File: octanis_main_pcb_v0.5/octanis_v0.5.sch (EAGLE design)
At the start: 78 parts, among them IC1 BME280, Q1 32.768kHz, Q2 32.768kHz, U3 DRV8836DSSR, U4 DRV8836DSSR, U5 DRV8836DSSR, U7 DRV8836DSSR

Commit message: rearranged GPIOs
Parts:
- removed C10: 4.7u, rcl:C-EUC0603
- removed C13: 220n, rcl:C-EUC0603
- removed C15: 100n, rcl:C-EUC0603
- removed COMPASS: HMC5883L, HMC5883L:HMC5883L
- removed GPIO1: A7:A0, pinhead:PINHD-1X8
- removed GPIO2: A18:A8, pinhead:PINHD-1X11
- added JP7: SPI, pinhead:PINHD-1X4
- added JP8: (no value), pinhead:PINHD-2X12
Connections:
- removed net N$14: GPIO2.1, MSP1.P4.5/A8
- removed net N$15: GPIO2.2, MSP1.P4.4/HSMCLK/SVMHOUT/A9
- removed net N$17: C10.1, COMPASS.C1
- removed net N$20: GPIO2.3, MSP1.P4.3/MCLK/RTCCLK/A10
- removed net N$21: GPIO2.4, MSP1.P4.2/ACLK/TA2CLK/A11
- removed net N$22: GPIO2.5, MSP1.P4.1/A12
- removed net N$23: GPIO2.6, MSP1.P4.0/A13
- removed net N$25: C13.2, COMPASS.SETP
- removed net N$27: GPIO1.1, MSP1.P5.5/A0
- removed net N$28: GPIO1.2, MSP1.P5.4/A1
- removed net N$30: GPIO1.3, MSP1.P5.3/A2
- removed net N$32: C13.1, COMPASS.SETC
- removed net N$35: GPIO1.4, MSP1.P5.2/A3
- removed net N$36: GPIO1.5, MSP1.P5.1/A4
- removed net N$37: GPIO1.6, MSP1.P5.0/A5
- removed net N$38: GPIO1.8, MSP1.P4.6/A7
- removed net N$43: GPIO1.7, MSP1.P4.7/A6
- new net A0: JP8.1, MSP1.P5.5/A0
- new net A1: JP8.2, MSP1.P5.4/A1
- new net A10: JP8.11, MSP1.P4.3/MCLK/RTCCLK/A10
- new net A11: JP8.12, MSP1.P4.2/ACLK/TA2CLK/A11
- new net A12: JP8.13, MSP1.P4.1/A12
- new net A13: JP8.14, MSP1.P4.0/A13
- new net A2: JP8.3, MSP1.P5.3/A2
- new net A23: JP8.24, MSP1.P8.2/TA3.2/A23
- new net A3: JP8.4, MSP1.P5.2/A3
- new net A4: JP8.5, MSP1.P5.1/A4
- new net A5: JP8.6, MSP1.P5.0/A5
- new net A6: JP8.7, MSP1.P4.7/A6
- new net A7: JP8.8, MSP1.P4.6/A7
- new net A8: JP8.9, MSP1.P4.5/A8
- new net A9: JP8.10, MSP1.P4.4/HSMCLK/SVMHOUT/A9
- net +3V3: no longer C15.2, COMPASS.S1, COMPASS.VDD, COMPASS.VDD_IO
- net A14: now also JP8.15; no longer GPIO2.7
- net A15: now also JP8.16; no longer GPIO2.8
- net A16: now also JP8.17; no longer GPIO2.9
- net A17: now also JP8.18; no longer GPIO2.10
- net A18: now also JP8.19; no longer GPIO2.11
- net A19: now also JP8.20
- net A20: now also JP8.21
- net A21: now also JP8.22
- net A22: now also JP8.23
- net GND: no longer C10.2, C15.1, COMPASS.GND
- net M5678SLEEP: now also MSP1.P2.0/PM_UCA1STE; no longer MSP1.P3.4/PM_UCB2STE
- net M7IN1: now also MSP1.P8.1/UCB3CLK/TA2.0/C0.0; no longer MSP1.P3.0/PM_UCA2STE
- net M7IN2: now also MSP1.P3.0/PM_UCA2STE; no longer MSP1.P8.1/UCB3CLK/TA2.0/C0.0
- net M8IN2: now also MSP1.P3.4/PM_UCB2STE; no longer MSP1.P8.2/TA3.2/A23
- net SCL: no longer COMPASS.SCL
- net SDA: no longer COMPASS.SDA
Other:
- note removed: "compass"

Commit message: separated motor supply. added pull ups for sleep pin
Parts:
- added R11, R12: 10k, rcl:R-EU_R0603
- added SJ6: (no value), jumper:SJ
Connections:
- new net V_MOTOR2: C26.2, C8.2, SJ6.1, U5.VCC, U7.VCC
- net +3V3: now also R11.2, R12.2
- net M1234SLEEP: now also R12.1
- net M5678SLEEP: now also R11.1
- net V_MOTOR: now also SJ6.2; no longer C26.2, C8.2, U5.VCC, U7.VCC
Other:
- moved on the sheet: C26, C27, C28, C29, C3, C4, C5, C6, C7, C8, IC1, JP4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

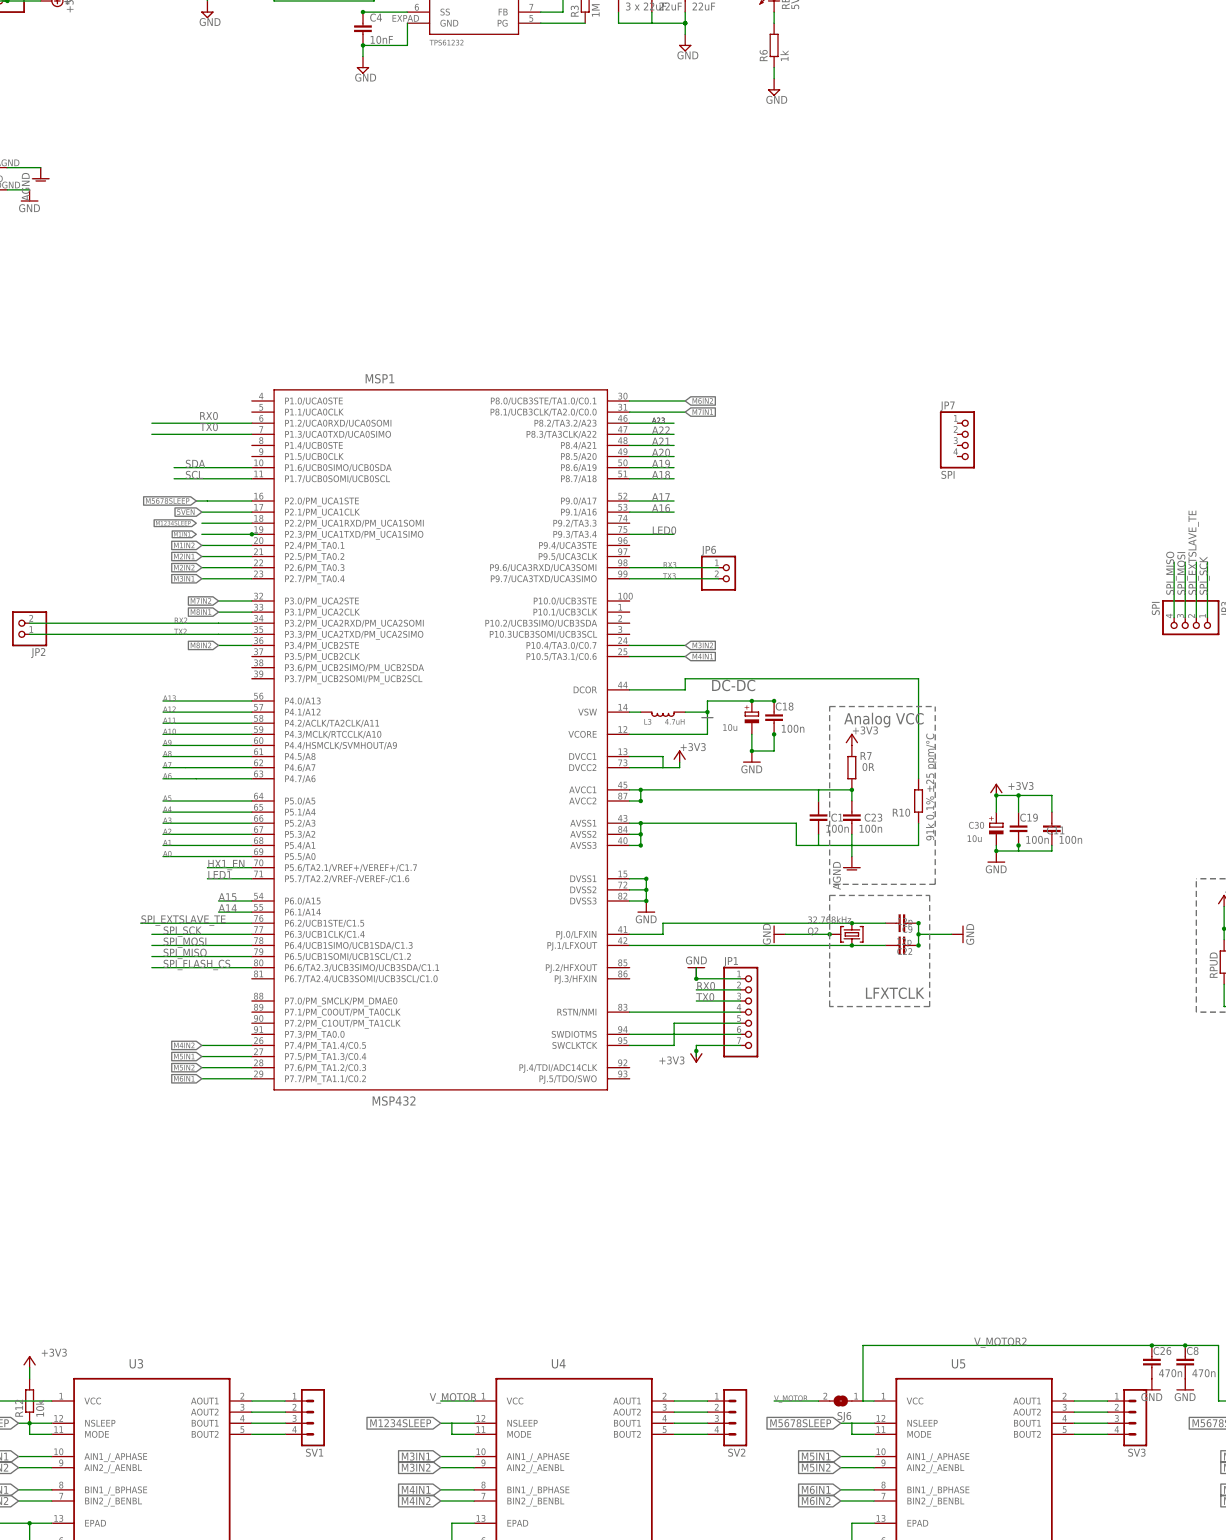
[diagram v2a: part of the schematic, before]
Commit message: redesigned hx1 pins
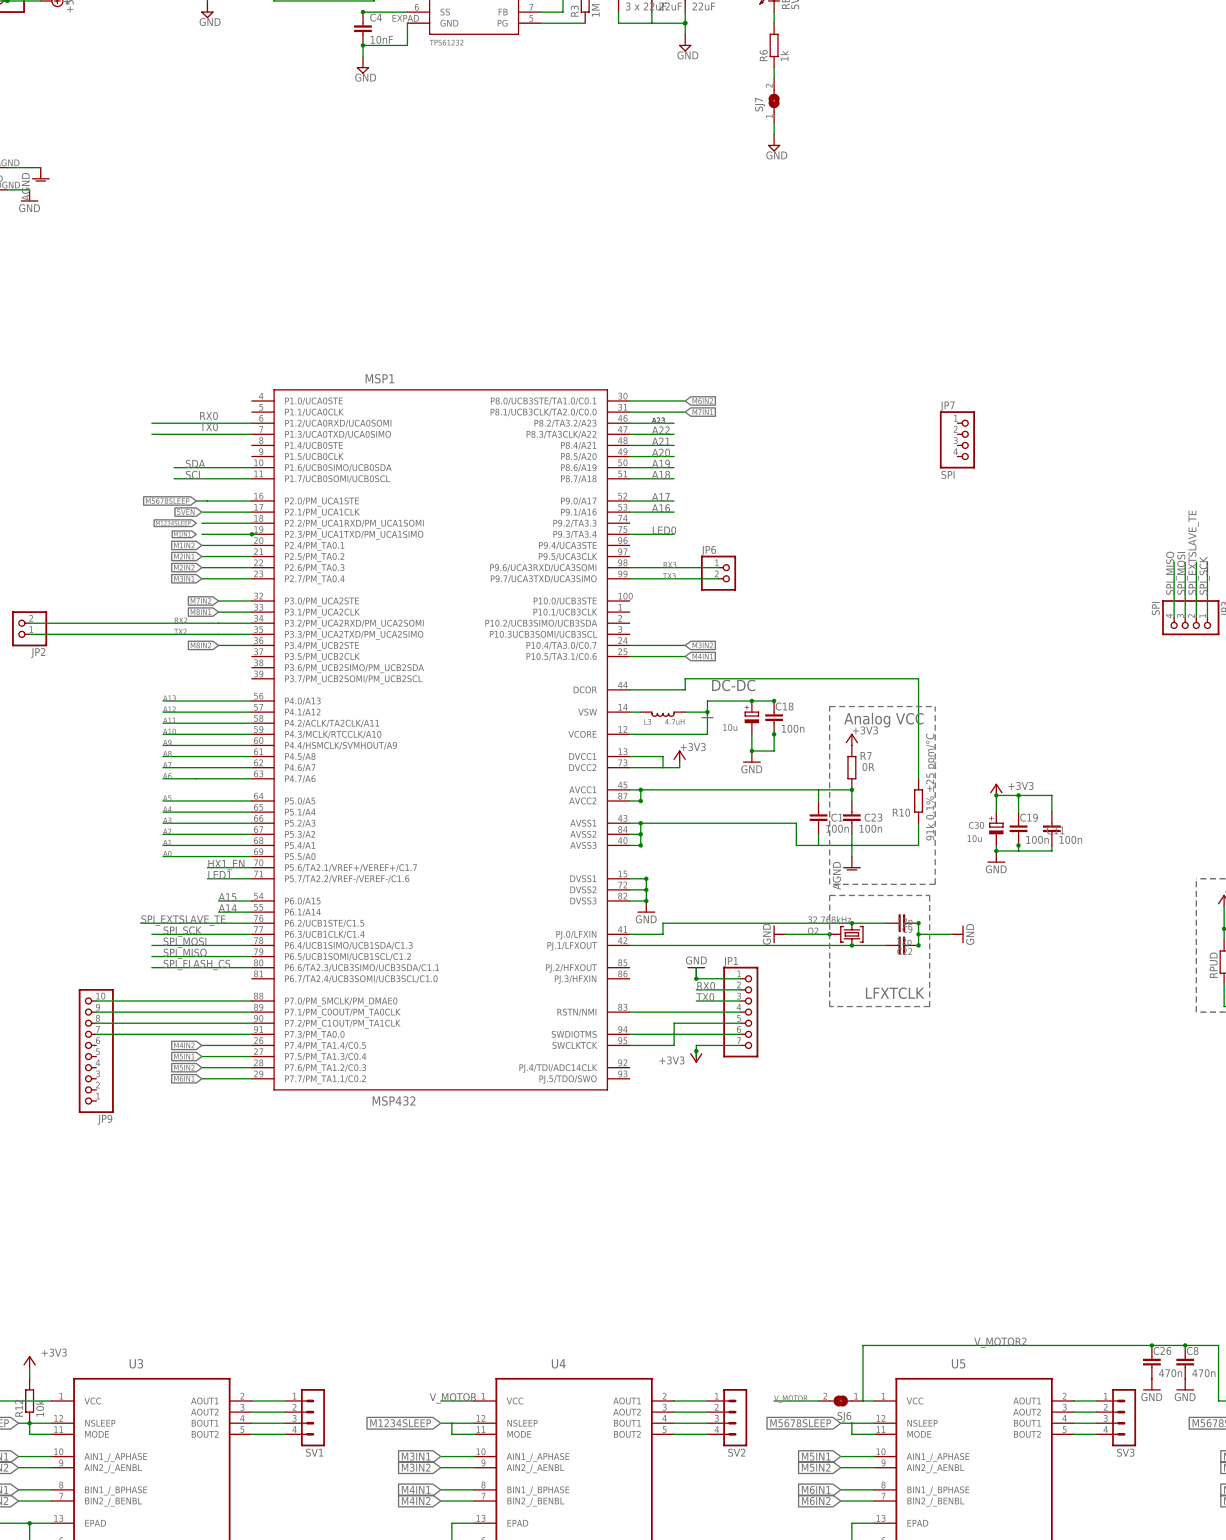
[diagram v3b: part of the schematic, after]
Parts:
- added JP9: (no value), pinhead:PINHD-1X10
- added SJ7: (no value), jumper:SJ
- U$4: value HX1 -> HX1EXTERNALMOUNT; device Octanis1:HX1 -> Octanis1:HX1EXTERNALMOUNT
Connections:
- new net N$14: R6.1, SJ7.2
- new net N$15: JP9.10, MSP1.P7.0/PM_SMCLK/PM_DMAE0
- new net N$17: JP9.9, MSP1.P7.1/PM_C0OUT/PM_TA0CLK
- new net N$20: JP9.8, MSP1.P7.2/PM_C1OUT/PM_TA1CLK
- new net N$21: JP9.7, MSP1.P7.3/PM_TA0.0
- net GND: now also SJ7.1; no longer R6.1
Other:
- moved on the sheet: SV3

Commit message: assigned all GPIO
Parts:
- removed JP2: (no value), pinhead:PINHD-1X2
- removed SJ4, SJ5: (no value), jumper:SJ
- added C10: 10u, rcl:CPOL-EUA/3216-18R
- added JP10: (no value), pinhead:PINHD-2X10
- JP3: value SPI -> (none); device pinhead:PINHD-1X4 -> pinhead:PINHD-2X2
- JP6: device pinhead:PINHD-1X2 -> pinhead:PINHD-2X2
- JP9: device pinhead:PINHD-1X10 -> pinhead:PINHD-2X2
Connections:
- removed net N$24: U$4.TXD
- removed net N$29: R8.1, SJ4.2
- removed net N$31: R9.1, SJ5.2
- new net HX1_DATA: MSP1.P1.4/UCB0STE, U$4.TXD
- new net P1.0: JP10.20, MSP1.P1.0/UCA0STE
- new net P1.1: JP10.19, MSP1.P1.1/UCA0CLK
- new net P10.2: JP10.17, MSP1.P10.2/UCB3SIMO/UCB3SDA
- new net P10.3: JP10.18, MSP1.P10.3UCB3SOMI/UCB3SCL
- new net P5.6: JP10.7, MSP1.P5.6/TA2.1/VREF+/VEREF+/C1.7
- new net P5.7: JP10.5, MSP1.P5.7/TA2.2/VREF-/VEREF-/C1.6
- new net P6.6: JP10.10, MSP1.P6.6/TA2.3/UCB3SIMO/UCB3SDA/C1.1
- new net P6.7: JP10.9, MSP1.P6.7/TA2.4/UCB3SOMI/UCB3SCL/C1.0
- new net P9.2: JP10.3, MSP1.P9.2/TA3.3
- new net P9.3: JP10.1, MSP1.P9.3/TA3.4
- new net P9.4: JP10.15, MSP1.P9.4/UCA3STE
- new net P9.5: JP10.16, MSP1.P9.5/UCA3CLK
- new net PJ.2: JP10.13, MSP1.PJ.2/HFXOUT
- new net PJ.3: JP10.14, MSP1.PJ.3/HFXIN
- new net PJ.4: JP10.11, MSP1.PJ.4/TDI/ADC14CLK
- new net PJ.5: JP10.12, MSP1.PJ.5/TDO/SWO
- net +3V3: now also JP6.1
- net +5V: now also C10.+, JP3.2
- net GND: now also JP3.4, JP6.3, R8.1, R9.1; no longer C2.2, SJ4.1, SJ5.1, U$4.0V
- net HX1_EN: now also MSP1.P1.5/UCB0CLK; no longer MSP1.P5.6/TA2.1/VREF+/VEREF+/C1.7
- net LED0: now also MSP1.P10.0/UCB3STE; no longer MSP1.P9.3/TA3.4
- net LED1: now also MSP1.P10.1/UCB3CLK; no longer MSP1.P5.7/TA2.2/VREF-/VEREF-/C1.6
- net N$15: now also JP10.2; no longer JP9.10
- net N$17: now also JP10.4; no longer JP9.9
- net N$19: now also Q1.2
- net N$20: now also JP10.6; no longer JP9.8
- net N$21: now also JP10.8; no longer JP9.7
- net RFGND: now also C10.-, C2.2, U$4.0V
- net RX2: now also JP6.2; no longer JP2.2
- net RX3: now also JP3.1; no longer JP6.1
- net SCL: now also JP4.1, JP5.3; no longer JP4.2, JP5.4
- net SDA: now also JP4.2, JP5.4; no longer JP4.1, JP5.3
- net SPI_EXTSLAVE_TE: now also JP9.1; no longer JP3.2
- net SPI_FLASH_CS: now also MSP1.P3.5/PM_UCB2CLK; no longer MSP1.P6.6/TA2.3/UCB3SIMO/UCB3SDA/C1.1
- net SPI_MISO: now also JP9.2; no longer JP3.4
- net SPI_MOSI: now also JP9.4; no longer JP3.3
- net SPI_SCK: now also JP9.3; no longer JP3.1
- net TX2: now also JP6.4; no longer JP2.1
- net TX3: now also JP3.3; no longer JP6.2
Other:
- note added: "Change history v0.5: --> SCHEMATIC: - added 10uF cap - connected 0V pin to RF GND - connected filter caps to RF GND --> LAYOUT: - Starground connection point placed directly at the supply pin. - Groundplane polygon around all pins with greater isolation space."
- moved on the sheet: JP3

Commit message: mainboard: digital gpio routed
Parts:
- removed JP10: (no value), pinhead:PINHD-2X10
- added C13: 100n, rcl:C-EUC0603
- added JP2: (no value), pinhead:PINHD-2X11
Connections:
- removed net 3.3V: U$3.WP
- removed net N$15: JP10.2, MSP1.P7.0/PM_SMCLK/PM_DMAE0
- removed net N$17: JP10.4, MSP1.P7.1/PM_C0OUT/PM_TA0CLK
- removed net N$20: JP10.6, MSP1.P7.2/PM_C1OUT/PM_TA1CLK
- removed net N$21: JP10.8, MSP1.P7.3/PM_TA0.0
- new net P3.6: JP2.5, MSP1.P3.6/PM_UCB2SIMO/PM_UCB2SDA
- new net P3.7: JP2.6, MSP1.P3.7/PM_UCB2SOMI/PM_UCB2SCL
- new net P7.0: JP2.12, MSP1.P7.0/PM_SMCLK/PM_DMAE0
- new net P7.1: JP2.11, MSP1.P7.1/PM_C0OUT/PM_TA0CLK
- new net P7.2: JP2.14, MSP1.P7.2/PM_C1OUT/PM_TA1CLK
- new net P7.3: JP2.13, MSP1.P7.3/PM_TA0.0
- net +3V3: now also C13.1, U$3.WP
- net GND: now also C13.2
- net P1.0: now also JP2.19; no longer JP10.20
- net P1.1: now also JP2.21; no longer JP10.19
- net P10.2: now also JP2.20; no longer JP10.17
- net P10.3: now also JP2.22; no longer JP10.18
- net P5.6: now also JP2.2; no longer JP10.7
- net P5.7: now also JP2.1; no longer JP10.5
- net P6.6: now also JP2.8; no longer JP10.10
- net P6.7: now also JP2.7; no longer JP10.9
- net P9.2: now also JP2.4; no longer JP10.3
- net P9.3: now also JP2.3; no longer JP10.1
- net P9.4: now also JP2.18; no longer JP10.15
- net P9.5: now also JP2.17; no longer JP10.16
- net PJ.2: now also JP2.10; no longer JP10.13
- net PJ.3: now also JP2.9; no longer JP10.14
- net PJ.4: now also JP2.16; no longer JP10.11
- net PJ.5: now also JP2.15; no longer JP10.12

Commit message: mainboard routing finished
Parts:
- removed JP7: SPI, pinhead:PINHD-1X4
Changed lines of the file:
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@@
 <part name="+3V19" library="supply1" deviceset="+3V3" device=""/>
 <part name="GND30" library="supply1" deviceset="GND" device=""/>
-<part name="JP7" library="pinhead" deviceset="PINHD-1X4" device="" value="SPI"/>
 <part name="JP8" library="pinhead" deviceset="PINHD-2X12" device=""/>
 <part name="+3V5" library="supply1" deviceset="+3V3" device=""/>
@@
 <instance part="+3V19" gate="G$1" x="828.04" y="210.82"/>
 <instance part="GND30" gate="1" x="833.12" y="114.3"/>
-<instance part="JP7" gate="A" x="450.85" y="327.66"/>
 <instance part="JP8" gate="A" x="190.5" y="248.92"/>
 <instance part="+3V5" gate="G$1" x="236.22" y="119.38" smashed="yes">

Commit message: mainboard finished
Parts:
- removed JP2: (no value), pinhead:PINHD-2X11
- removed JP3: (no value), pinhead:PINHD-2X2
- removed U$3: SST25VF064C, BertaLib:SST25VF064C
- added BLP, RST: PTR1B1,27, testpad:PTR1B1,27
- added DIGITAL_IO: (no value), pinhead:PINHD-2X11
- added RX3/TX3: (no value), pinhead:PINHD-2X2
- added U6: DRV8836DSSR, DRV8834:DRV8836DSSR
- U7: value DRV8836DSSR -> SST25VF064C; device DRV8834:DRV8836DSSR -> BertaLib:SST25VF064C
- renumbered GREEN to 3V, JP1 to PROG, JP6 to RX2/TX2, JP8 to ANALOG_IO, JP9 to SPI, L3 to L2, MSP1 to U1, RED to 5V, U$1 to U2, U$5 to IC2
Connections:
- removed net P5.6: JP2.2, U1.P5.6/TA2.1/VREF+/VEREF+/C1.7
- removed net P5.7: JP2.1, U1.P5.7/TA2.2/VREF-/VEREF-/C1.6
- net +3V3: now also DIGITAL_IO.1, RX2/TX2.3, RX3/TX3.3, U7.HOLD, U7.VCC, U7.WP; no longer RX2/TX2.1, U$3.HOLD, U$3.VCC, U$3.WP
- net +5V: no longer JP3.2
- net ACCEL_INT: now also U1.P3.5/PM_UCB2CLK
- net ACCEL_N_BOOTLD: now also BLP.TP
- net ACCEL_N_RST: now also RST.TP
- net GND: now also DIGITAL_IO.2, RX2/TX2.1, RX3/TX3.1, U1.P5.7/TA2.2/VREF-/VEREF-/C1.6, U2.GND1, U2.GND2, U2.GND3, U2.GND4, U2.GND5, U6.EPAD, U6.GND; no longer JP3.4, RX2/TX2.3, U$3.GND, U7.EPAD
- net M5678SLEEP: now also U6.MODE, U6.NSLEEP; no longer U7.MODE, U7.NSLEEP
- net M7IN1: now also U6.AIN1_/_APHASE; no longer U7.AIN1_/_APHASE
- net M7IN2: now also U6.AIN2_/_AENBL; no longer U7.AIN2_/_AENBL
- net M8IN1: now also U6.BIN1_/_BPHASE; no longer U7.BIN1_/_BPHASE
- net M8IN2: now also U6.BIN2_/_BENBL; no longer U7.BIN2_/_BENBL
- net N$53: now also U6.AOUT1; no longer U7.AOUT1
- net N$54: now also U6.AOUT2; no longer U7.AOUT2
- net N$55: now also U6.BOUT1; no longer U7.BOUT1
- net N$56: now also U6.BOUT2; no longer U7.BOUT2
- net P1.0: now also DIGITAL_IO.19; no longer JP2.19
- net P1.1: now also DIGITAL_IO.21; no longer JP2.21
- net P10.2: now also DIGITAL_IO.20; no longer JP2.20
- net P10.3: now also DIGITAL_IO.22; no longer JP2.22
- net P3.6: now also DIGITAL_IO.5; no longer JP2.5
- net P3.7: now also DIGITAL_IO.6; no longer JP2.6
- net P6.6: now also DIGITAL_IO.8; no longer JP2.8
- net P6.7: now also DIGITAL_IO.7; no longer JP2.7
- net P7.0: now also DIGITAL_IO.12; no longer JP2.12
- net P7.1: now also DIGITAL_IO.11; no longer JP2.11
- net P7.2: now also DIGITAL_IO.14; no longer JP2.14
- net P7.3: now also DIGITAL_IO.13; no longer JP2.13
- net P9.2: now also DIGITAL_IO.4; no longer JP2.4
- net P9.3: now also DIGITAL_IO.3; no longer JP2.3
- net P9.4: now also DIGITAL_IO.18; no longer JP2.18
- net P9.5: now also DIGITAL_IO.17; no longer JP2.17
- net PJ.2: now also DIGITAL_IO.10; no longer JP2.10
- net PJ.3: now also DIGITAL_IO.9; no longer JP2.9
- net PJ.4: now also DIGITAL_IO.16; no longer JP2.16
- net PJ.5: now also DIGITAL_IO.15; no longer JP2.15
- net RX3: now also RX3/TX3.2; no longer JP3.1
- net SPI_FLASH_CS: now also U1.P5.6/TA2.1/VREF+/VEREF+/C1.7, U7.CS; no longer U$3.CS, U1.P3.5/PM_UCB2CLK
- net SPI_MISO: now also U7.MISO; no longer U$3.MISO
- net SPI_MOSI: now also U7.MOSI; no longer U$3.MOSI
- net SPI_SCK: now also U7.SCK; no longer U$3.SCK
- net TX3: now also RX3/TX3.4; no longer JP3.3
- net V_MOTOR2: now also U6.VCC; no longer U7.VCC
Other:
- note added: "VeREF- (recommended to connect to GND)"
